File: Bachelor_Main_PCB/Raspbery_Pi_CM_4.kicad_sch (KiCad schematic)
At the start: 6 parts, among them J21 M20-9990245, Q2 SSM3J358R,LF, U1 SC0683, X1 DF40HC_3.0_-100DS-0.4V_58, X2 DF40HC_3.0_-100DS-0.4V_58

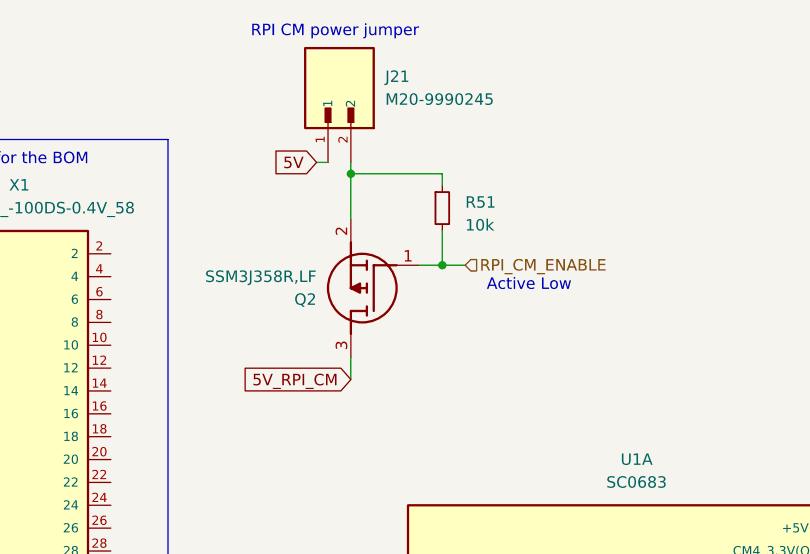
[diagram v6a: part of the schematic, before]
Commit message: Remove RPI CM power on mosfet. Replaced with EN pin to PSU
the pin is now routed instead to the LMR51450 converter ENABLE pin.
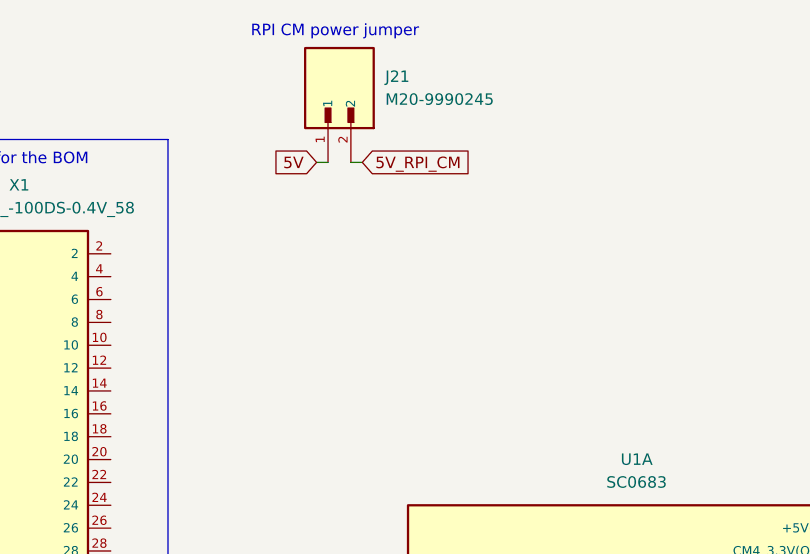
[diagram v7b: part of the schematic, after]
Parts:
- removed Q2: SSM3J358R,LF, KiCad4:SOTFL95P240X88-3N, symbol SSM3J358R_LF:SSM3J358R,LF
- removed R51: 10k, Resistor_SMD:R_0402_1005Metric, symbol Device:R_Small
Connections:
- net 5V_RPI_CM: now also J21.2
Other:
- note removed: "Active Low"

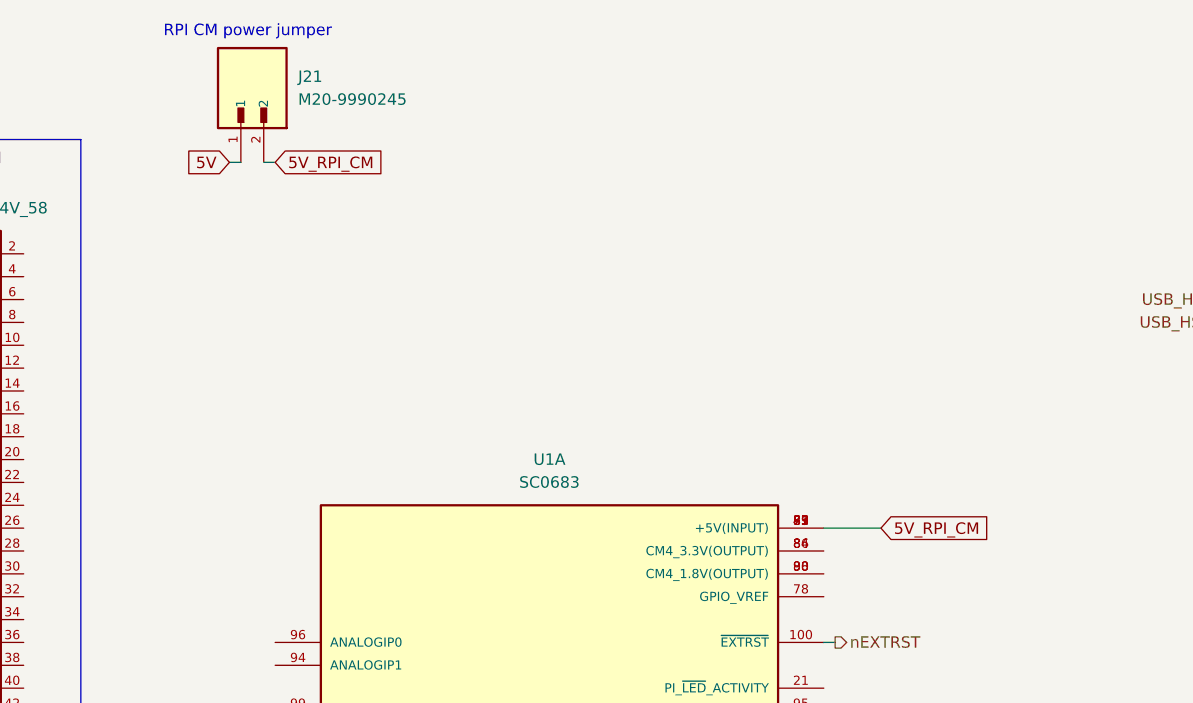
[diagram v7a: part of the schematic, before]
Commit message: Add series inductors to switch mode convertors. Add screw terminal
For the audiomoth power.
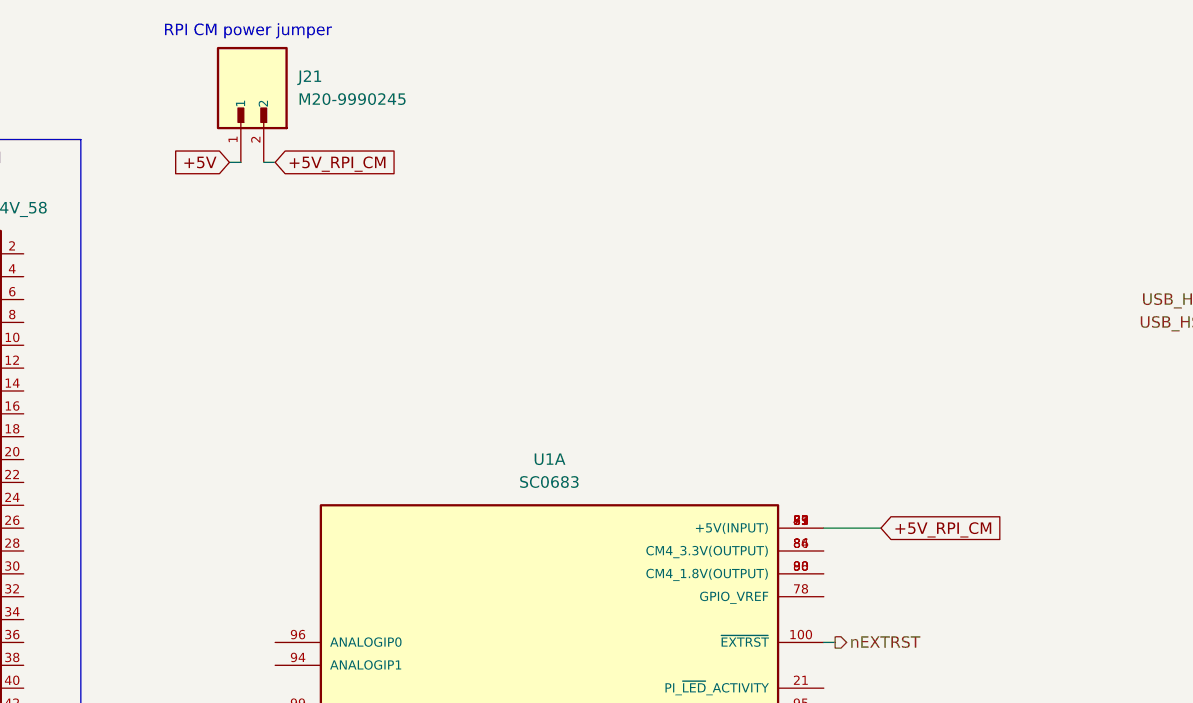
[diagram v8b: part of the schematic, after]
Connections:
- net 5V renamed +5V
- net 5V_RPI_CM renamed +5V_RPI_CM
